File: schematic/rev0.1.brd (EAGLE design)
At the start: 63.9 x 69.8 mm, 40 parts, among them IC1 L293DD, IC2 L293DD, IC3 L293DD, IC4 L293D, J1 USB_B_PTH, Q1 600mA/40V, U1 DS1307Z, Y1 32.768kHz, Y2 16MHz

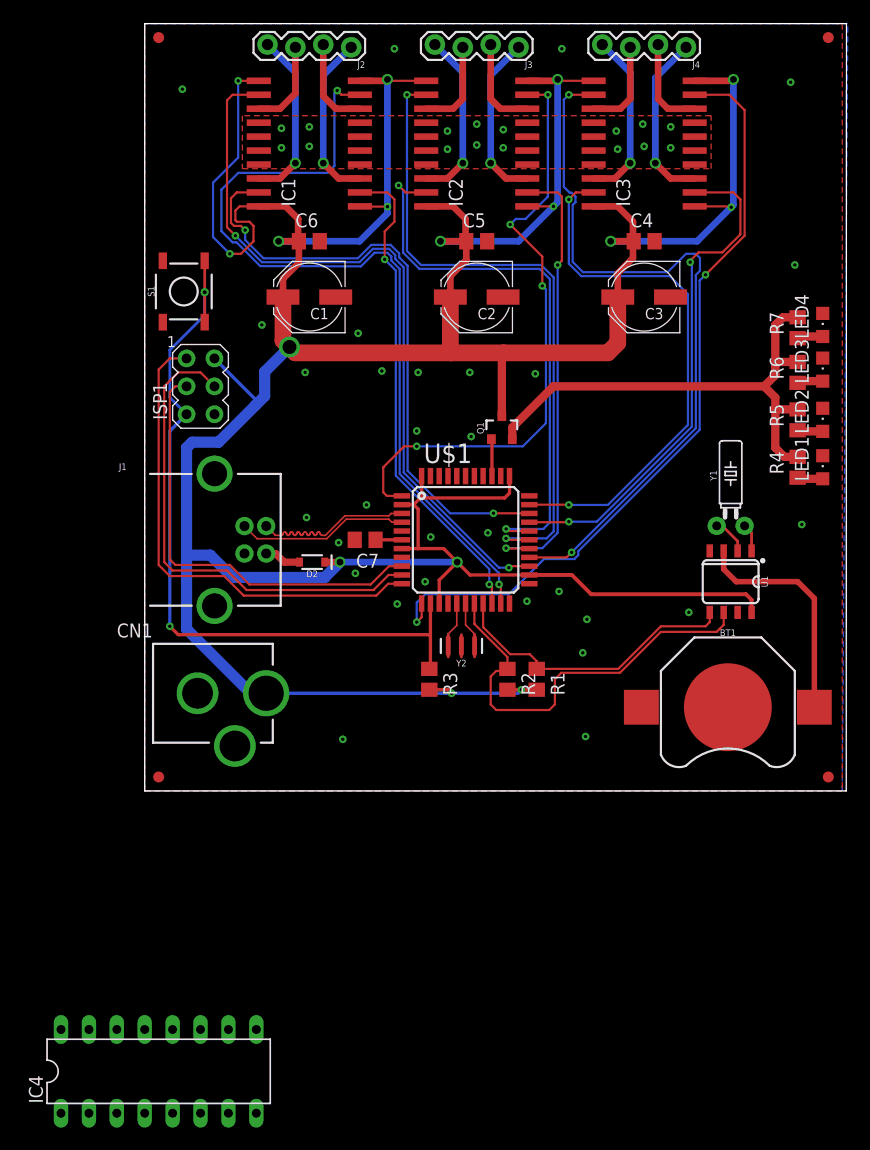
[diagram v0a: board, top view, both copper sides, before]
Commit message: closer to done
changed the motor to be driven by 12vin, inserted voltage regulator to have one power supply, constant enable. would like to condence the design a little.
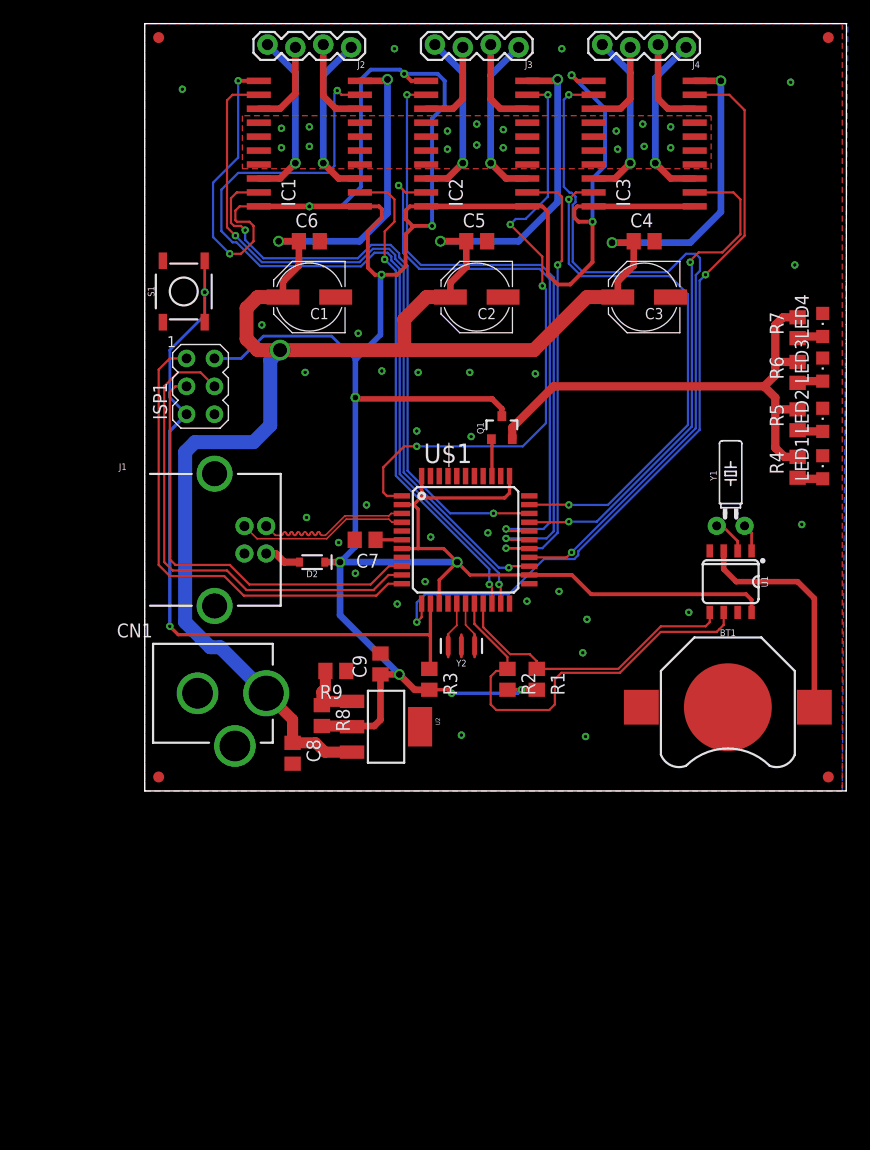
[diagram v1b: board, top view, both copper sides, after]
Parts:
- removed IC4: L293D, st-microelectronics:DIL16
- added C8: 0.1uF, resistor:C0805
- added C9: 10uF, resistor:C0805
- added R8: 1K, resistor:R0805
- added R9: 3K, resistor:R0805
- added U2: V_REG_317SMD, SparkFun-IC-Power:SOT223
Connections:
- removed net GND1: IC4.4
- removed net GND2: IC4.5
- removed net GND3: IC4.13
- removed net GND4: IC4.12
- removed net N$33: IC4.2
- removed net N$34: IC4.7
- removed net N$35: IC4.10
- removed net N$36: IC4.15
- removed net VCC1: IC4.16
- removed net VCC2: IC4.8
- new net 12V: C1.+, C2.+, C3.+, C4.1, C5.1, C6.1, C8.1, CN1.PWR, IC1.10, IC2.10, IC3.10, U2.3
- new net N$27: R8.1, R9.2, U2.1
- net GND: now also C8.2, C9.2, R9.1
- net VCC: now also C9.1, R8.2, U2.2; no longer C1.+, C2.+, C3.+, C4.1, C5.1, C6.1, CN1.PWR, IC1.10, IC2.10, IC3.10
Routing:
- net 12V: track 0.00 -> 203.9 mm, vias 0 -> 7
- net VCC: track 374.4 -> 320.0 mm, vias 16 -> 14
- net N$27: track 0.00 -> 6.13 mm

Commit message: clean up
clean up
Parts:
- added SJ1, SJ2: (no value), jumper:SJ
- moved U$5 1.03 mm to (2.00, 2.00)
- moved U$3 0.93 mm to (2.00, 68.0)
- moved U$4 0.77 mm to (62.0, 2.00)
- moved C8 0.68 mm to (12.8, 3.68)
- moved CN1 0.63 mm to (-3.17, 8.89)
- moved U$2 0.62 mm to (62.0, 68.0)
- renumbered U$1 to U3
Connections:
- new net N$13: SJ2.2, U2.3
- net 12V: now also SJ1.1, SJ2.1; no longer U2.3
- net VCC: now also SJ1.2
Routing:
- net N$13: track 0.00 -> 3.31 mm
- net VCC: track 320.0 -> 322.8 mm
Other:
- board size 63.9 x 69.8 mm -> 64 x 70 mm
- board text added: "CLOCK"
- board text added: "EARTH CLOCK"
- board text added: "LUNAR"
- board text added: "REV0.1"
- board text added: "SCOTT RYAN"
- board text added: "TIDE"
- board text added: "alleybeacheelctric@gmail.com"
